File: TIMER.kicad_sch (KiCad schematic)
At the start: 9 parts

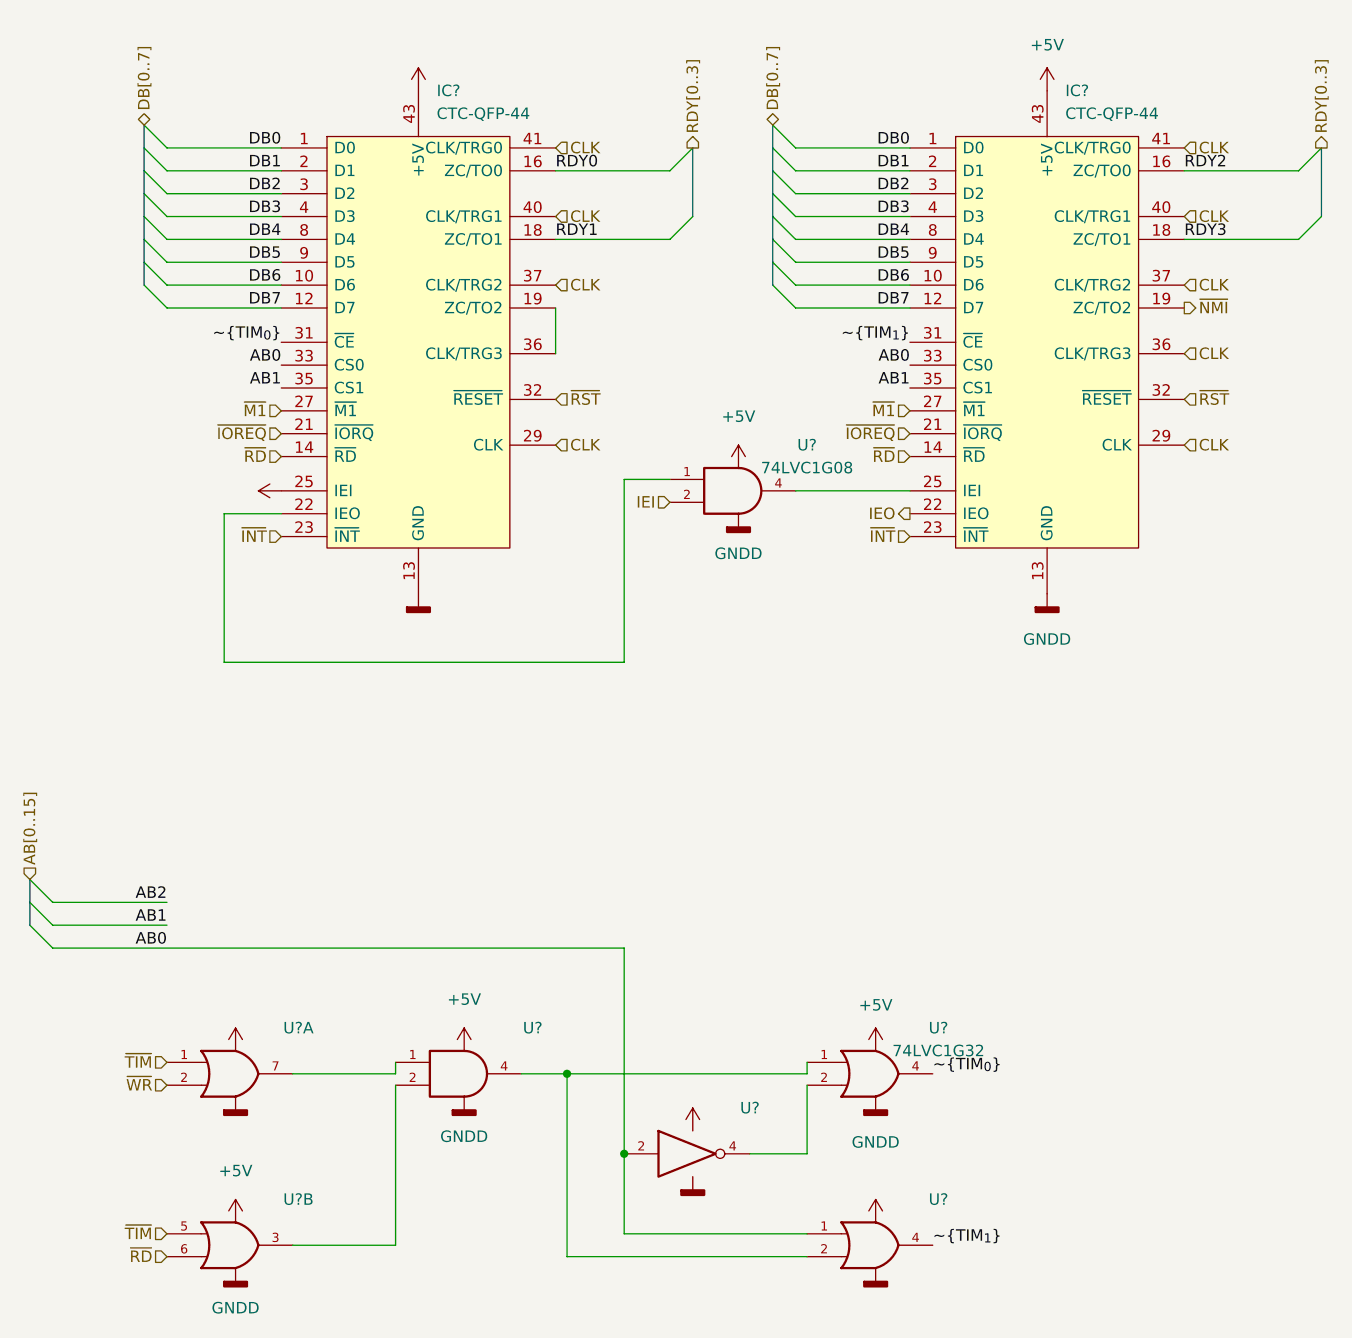
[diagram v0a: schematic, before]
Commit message: updated 84c10 pinout, apparently never checked for validity.... further simplification of dma and timer system (removed mode 2 interrupt structure, and interrupts in general) cleaned up vhdl code for 1508, still need testing to ensure functionality and that it even fits in the 1508....
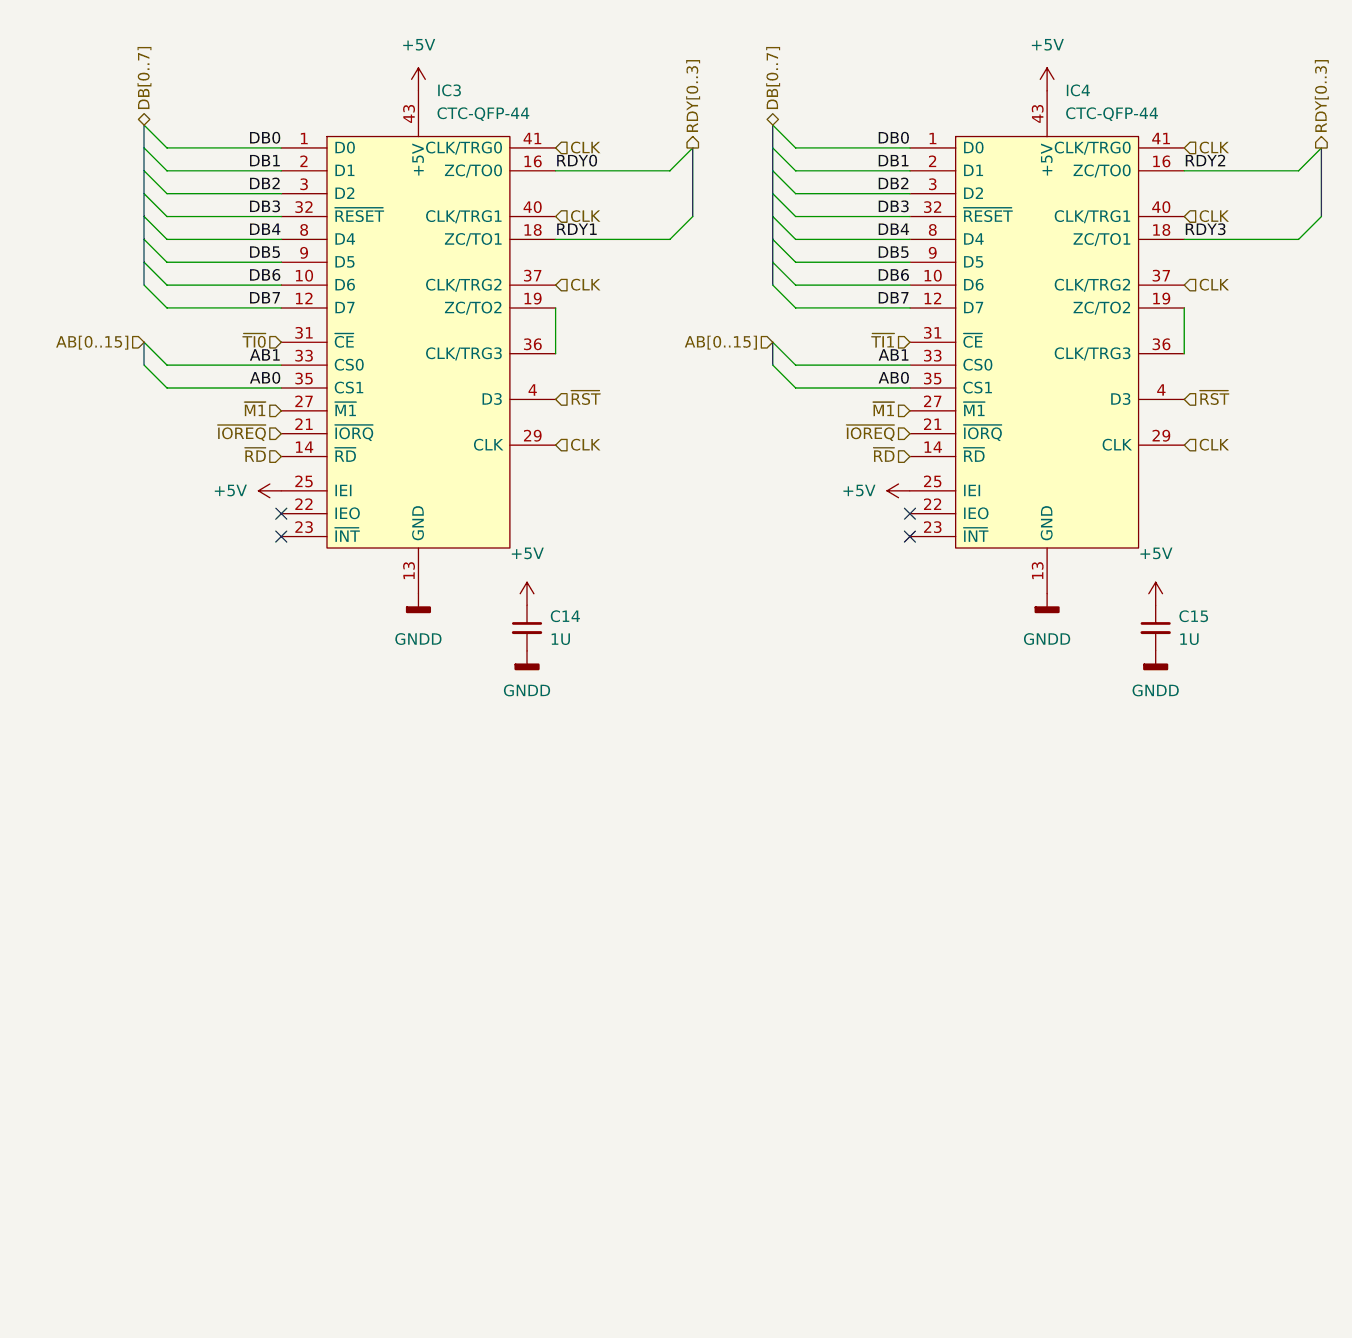
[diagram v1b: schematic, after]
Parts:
- removed U?: (no value), symbol 74xGxx:74LVC1G32
- removed U? (x2): (no value), symbol 74xGxx:74LVC2G32
- removed U?: (no value), symbol 74xGxx:74LVC1G04
- removed U?: 74LVC1G08, symbol 74xGxx:74LVC1G08
- removed U?: 74LVC1G32, symbol 74xGxx:74LVC1G32
- removed U?: (no value), symbol 74xGxx:74LVC1G08
- added C14, C15: 1U, Capacitor_SMD:C_1206_3216Metric, symbol Device:C_Small
- gave numbers to parts that had none: 2
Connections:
- net +5V: now also IC4.25 (IEI), C14.1, C15.1
- net AB0: now also IC3.35 (CS1), IC4.35 (CS1); no longer IC3.33 (CS0), IC4.33 (CS0)
- net AB1: now also IC3.33 (CS0), IC4.33 (CS0); no longer IC3.35 (CS1), IC4.35 (CS1)
- net CLK: no longer IC4.36 (CLK/TRG3)
- net DB3: now also IC3.32 (~{RESET}), IC4.32 (~{RESET}); no longer IC3.4 (D3), IC4.4 (D3)
- net ~{RST}: now also IC3.4 (D3), IC4.4 (D3); no longer IC3.32 (~{RESET}), IC4.32 (~{RESET})
- net GND renamed GNDD
- net GNDD: now also C14.2, C15.2
- net IEO: no longer names the net of IC4.22 (IEO)
- net ~{INT}: no longer names the net of IC3.23 (~{INT})
- net ~{INT}: no longer IC4.23 (~{INT})
- net ~{NMI}: no longer names the net of IC4.19 (ZC/TO2)
- net ~{NMI}: now also IC4.36 (CLK/TRG3)
- net ~{TIM_{0}} renamed ~{TI0}
- net ~{TIM_{1}} renamed ~{TI1}
- no-connect marks 0 -> 4
